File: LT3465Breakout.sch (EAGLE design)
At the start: 39 parts

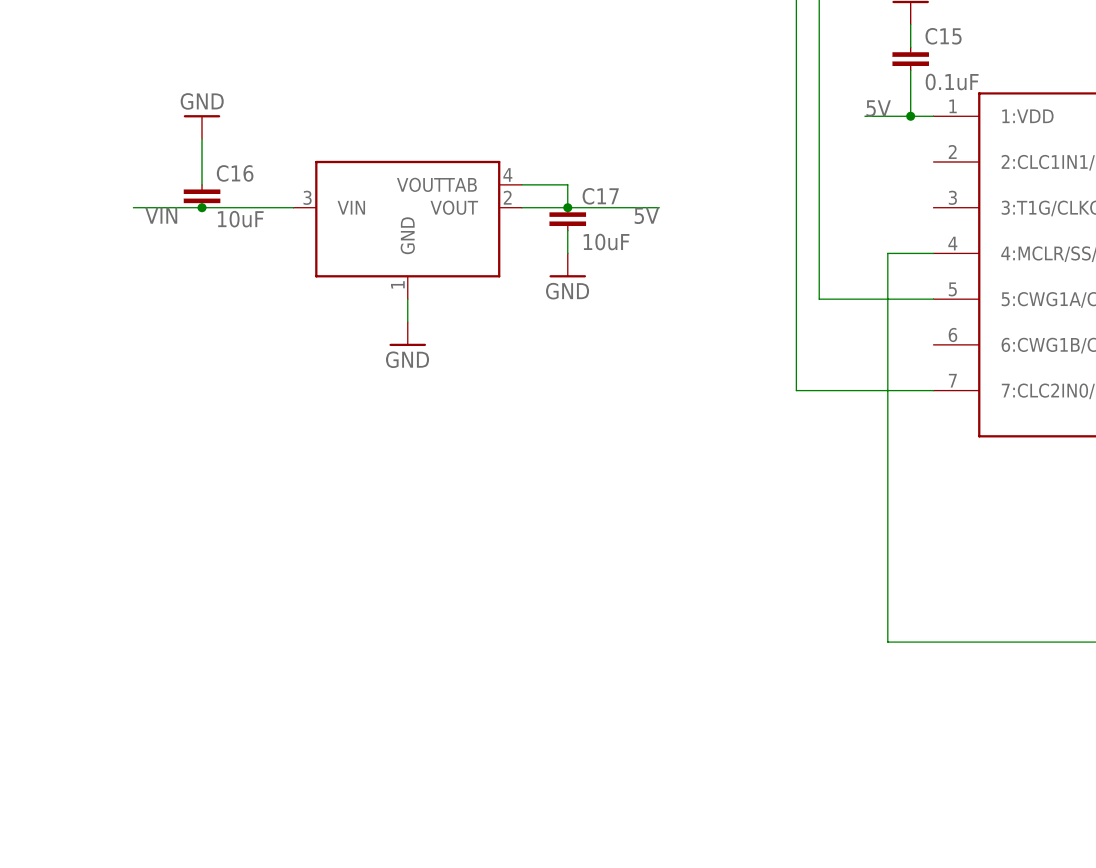
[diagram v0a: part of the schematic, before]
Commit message: Added comm header, general cleanup, more labels.
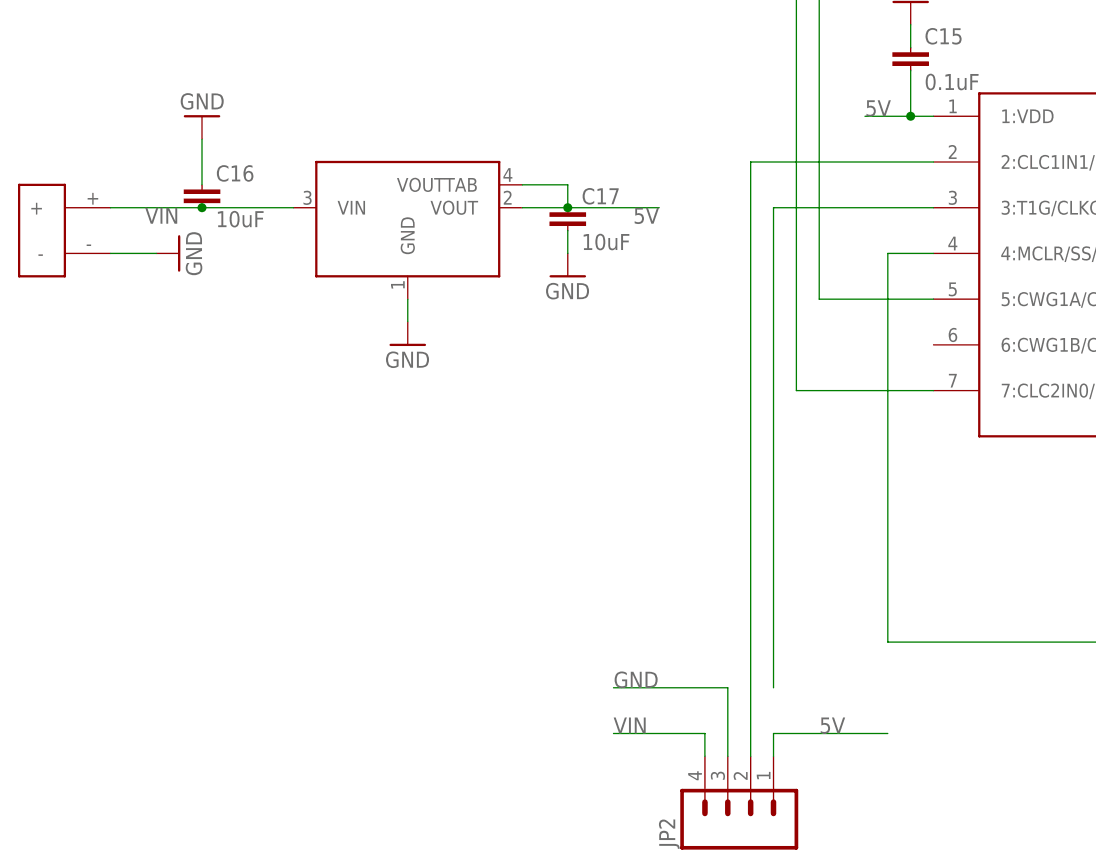
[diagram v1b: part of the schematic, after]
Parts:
- added JP2: (no value), 1dah:M04LOCK
- added U$17: POWER_SOLDER-1.5, 1dah:POWER_SOLDER-1.5
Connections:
- new net N$1: U$2.3:T1G/CLKOUT/SDO/NCO1/AN3/RA4
- new net N$2: JP2.2, U$2.2:CLC1IN1/NCO1CLK/T1CKI/CLKIN/RA5
- net 5V: now also JP2.1
- net GND: now also JP2.3, U$17.-
- net VIN: now also JP2.4, U$17.+
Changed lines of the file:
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@@
 <?xml version="1.0" encoding="utf-8"?>
 <!DOCTYPE eagle SYSTEM "eagle.dtd">
-<eagle version="6.0">
+<eagle version="6.1">
 <drawing>
 <settings>
@@
 <part name="GND21" library="1dah" deviceset="GND" device=""/>
 <part name="GND22" library="1dah" deviceset="GND" device=""/>
+<part name="GND23" library="1dah" deviceset="GND" device=""/>
+<part name="U$17" library="1dah" deviceset="POWER_SOLDER" device="-1.5"/>
+<part name="JP2" library="1dah" deviceset="M04" device="LOCK"/>
 </parts>
 <sheets>
@@
 <instance part="GND21" gate="1" x="-119.38" y="-76.2" rot="R180"/>
 <instance part="GND22" gate="1" x="-78.74" y="-93.98"/>
+<instance part="GND23" gate="1" x="-121.92" y="-91.44" rot="R90"/>
+<instance part="U$17" gate="G$1" x="-137.16" y="-88.9" rot="R270"/>
+<instance part="JP2" gate="G$1" x="-58.42" y="-152.4" rot="R90"/>
 </instances>
 <busses>
@@
 <wire x1="-119.38" y1="-78.74" x2="-119.38" y2="-83.82" width="0.1524" layer="91"/>
 </segment>
+<segment>
+<pinref part="U$17" gate="G$1" pin="-"/>
+<pinref part="GND23" gate="1" pin="GND"/>
+<wire x1="-124.46" y1="-91.44" x2="-129.54" y2="-91.44" width="0.1524" layer="91"/>
+</segment>
+<segment>
+<pinref part="JP2" gate="G$1" pin="3"/>
+<wire x1="-60.96" y1="-147.32" x2="-60.96" y2="-139.7" width="0.1524" layer="91"/>
+<wire x1="-60.96" y1="-139.7" x2="-73.66" y2="-139.7" width="0.1524" layer="91"/>
+<label x="-73.66" y="-139.7" size="1.778" layer="95"/>
+</segment>
 </net>
 <net name="5V" class="0">
@@
 <pinref part="C17" gate="G$1" pin="1"/>
 <label x="-68.58" y="-86.36" size="1.778" layer="95" rot="R180"/>
+</segment>
+<segment>
+<pinref part="JP2" gate="G$1" pin="1"/>
+<wire x1="-55.88" y1="-147.32" x2="-55.88" y2="-144.78" width="0.1524" layer="91"/>
+<wire x1="-55.88" y1="-144.78" x2="-43.18" y2="-144.78" width="0.1524" layer="91"/>
+<label x="-50.8" y="-144.78" size="1.778" layer="95"/>
 </segment>
 </net>
@@
 <wire x1="-109.22" y1="-86.36" x2="-119.38" y2="-86.36" width="0.1524" layer="91"/>
 <junction x="-119.38" y="-86.36"/>
-<wire x1="-119.38" y1="-86.36" x2="-127" y2="-86.36" width="0.1524" layer="91"/>
+<wire x1="-119.38" y1="-86.36" x2="-129.54" y2="-86.36" width="0.1524" layer="91"/>
 <pinref part="C16" gate="G$1" pin="2"/>
 <label x="-121.92" y="-86.36" size="1.778" layer="95" rot="R180"/>
+<pinref part="U$17" gate="G$1" pin="+"/>
+</segment>
+<segment>
+<pinref part="JP2" gate="G$1" pin="4"/>
+<wire x1="-63.5" y1="-147.32" x2="-63.5" y2="-144.78" width="0.1524" layer="91"/>
+<wire x1="-63.5" y1="-144.78" x2="-73.66" y2="-144.78" width="0.1524" layer="91"/>
+<label x="-73.66" y="-144.78" size="1.778" layer="95"/>
 </segment>
 </net>
@@
 </segment>
 </net>
+<net name="N$1" class="0">
+<segment>
+<pinref part="U$2" gate="G$1" pin="3:T1G/CLKOUT/SDO/NCO1/AN3/RA4"/>
+<wire x1="-38.1" y1="-86.36" x2="-55.88" y2="-86.36" width="0.1524" layer="91"/>
+<wire x1="-55.88" y1="-86.36" x2="-55.88" y2="-139.7" width="0.1524" layer="91"/>
+</segment>
+</net>
+<net name="N$2" class="0">
+<segment>
+<pinref part="U$2" gate="G$1" pin="2:CLC1IN1/NCO1CLK/T1CKI/CLKIN/RA5"/>
+<wire x1="-38.1" y1="-81.28" x2="-58.42" y2="-81.28" width="0.1524" layer="91"/>
+<wire x1="-58.42" y1="-81.28" x2="-58.42" y2="-147.32" width="0.1524" layer="91"/>
+<pinref part="JP2" gate="G$1" pin="2"/>
+</segment>
+</net>
